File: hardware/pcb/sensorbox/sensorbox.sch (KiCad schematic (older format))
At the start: 4 parts, among them U1 NodeMCU_D1, U2 MH-Z14A, U3 BME280, U4 OLED-Display-0.69

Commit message: Final pcb design
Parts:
- added D1, D2, D3: LED, LED_THT:LED_D3.0mm, symbol Device:LED
- added Q1, Q2, Q3: 2N7002, Package_TO_SOT_SMD:SOT-23, symbol Transistor_FET:2N7002
- added R1, R2: 4.7k, Resistor_SMD:R_0805_2012Metric, symbol Device:R
- added R3, R4, R5: 330, Resistor_SMD:R_0805_2012Metric, symbol Device:R
- added SW1: Dark Mode, Button_Switch_THT:SW_PUSH_6mm, symbol Switch:SW_Push
- added U5: OLED-Display-0.69, sensorbox:OLED-Display-0.69, symbol sensorbox:OLED-Display-0.69
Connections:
- net 3V3: now also R1.1, R2.1, U5.2 (VCC)
- net 5V: now also U1.1 (5V), R3.1, R4.1, R5.1
- net GND: now also U1.2 (GND), Q1.2 (S), Q2.2 (S), Q3.2 (S), SW1.1, U5.1 (GND)
- net SCL: now also R2.2, U5.3 (SCL)
- net SDA: now also R1.2, U5.4 (SDA)
- net RED: now reaches U1.11 (D0)
- net RED: now also Q3.1 (G)
- net YELLOW: now reaches U1.12 (D5)
- net YELLOW: now also Q2.1 (G)
- net GREEN: now reaches U1.13 (D6)
- net GREEN: now also Q1.1 (G)
- net DARK: now reaches U1.4 (D3)
- net DARK: now also SW1.2
- new net: D3.1 (K), Q3.3 (D)
- new net: D3.2 (A), R5.2
- new net: D1.1 (K), Q1.3 (D)
- new net: D1.2 (A), R3.2
- new net: D2.1 (K), Q2.3 (D)
- new net: D2.2 (A), R4.2
- no-connect marks 0 -> 17
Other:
- moved on the sheet: U3

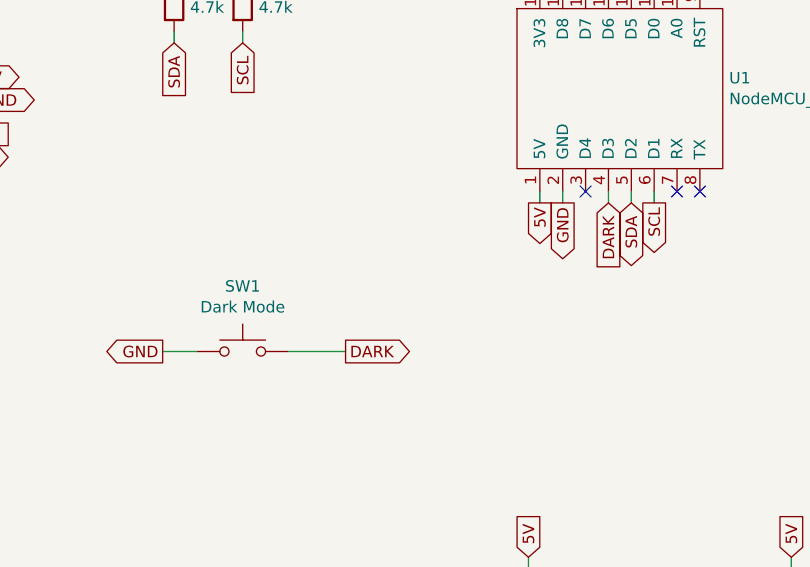
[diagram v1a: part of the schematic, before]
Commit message: Board redesign
- Move BME280 far away from MCU
- Move display, LEDs and button next to each other
- Rotate MCU to route cable out towards the bottom
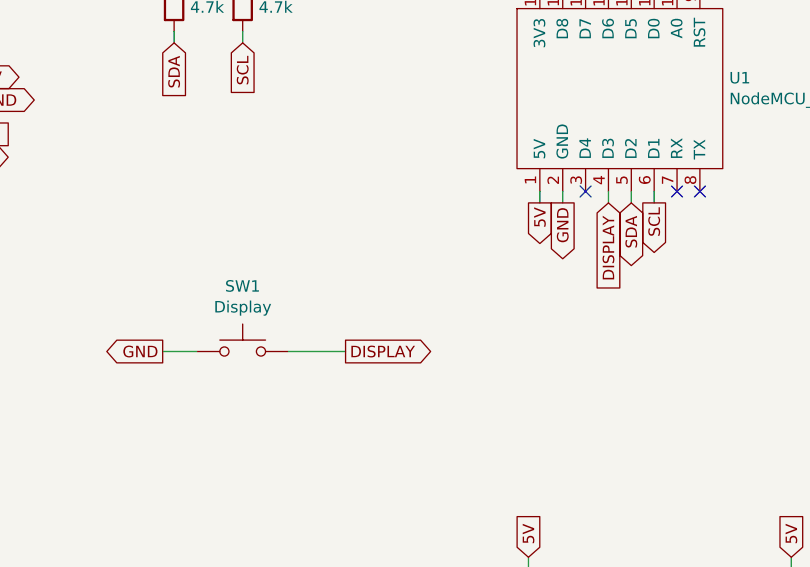
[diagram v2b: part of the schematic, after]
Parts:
- SW1: value Dark Mode -> Display
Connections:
- net DARK renamed DISPLAY
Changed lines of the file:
@@
 P 3450 3150
 F 0 "SW1" H 3450 3435 50  0000 C CNN
-F 1 "Dark Mode" H 3450 3344 50  0000 C CNN
+F 1 "Display" H 3450 3344 50  0000 C CNN
 F 2 "Button_Switch_THT:SW_PUSH_6mm" H 3450 3350 50  0001 C CNN
 F 3 "~" H 3450 3350 50  0001 C CNN
@@
 	3100 3150 3250 3150
 Text GLabel 3900 3150 2    50   Output ~ 0
-DARK
+DISPLAY
 Text GLabel 5050 2500 3    50   Input ~ 0
-DARK
+DISPLAY
 Wire Wire Line
 	5050 2450 5050 2500
